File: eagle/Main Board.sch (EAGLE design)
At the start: 3 parts

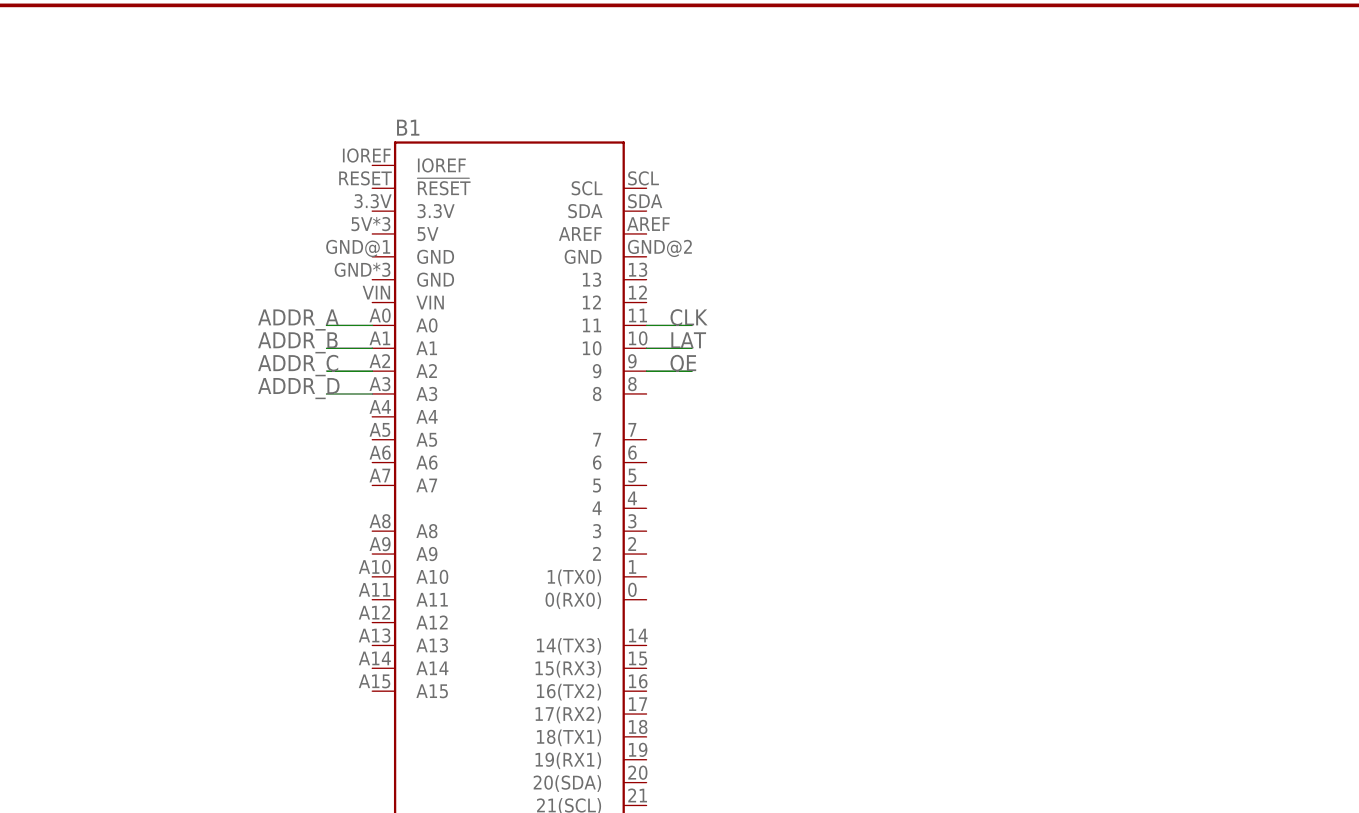
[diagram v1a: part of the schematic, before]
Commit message: Wired rotary encoder to arduino.
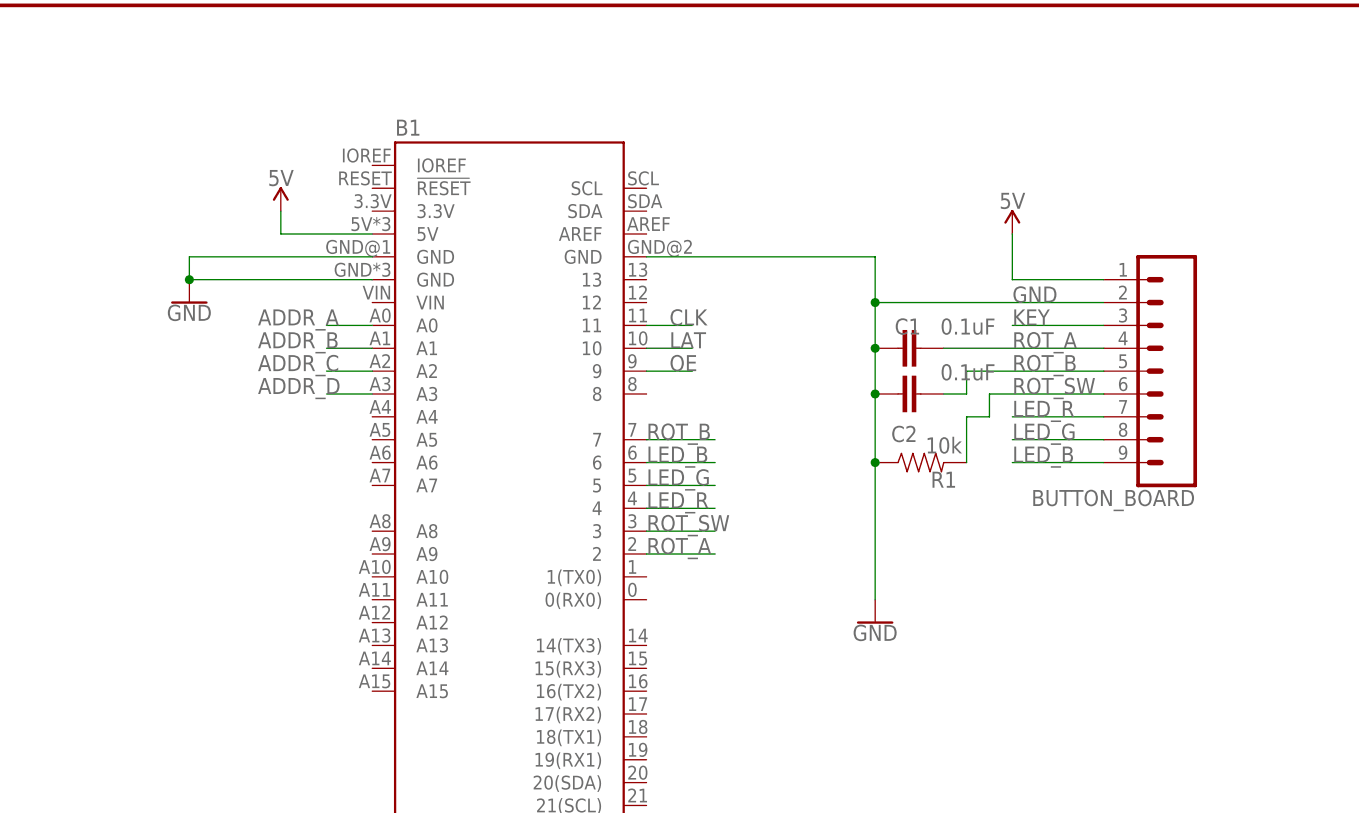
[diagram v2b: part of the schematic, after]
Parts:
- added BUTTON_BOARD: (no value), SparkFun-Connectors:CONN_09
- added C1, C2: 0.1uF, SparkFun-Capacitors:0.1UF-KIT-EZ-50V-20%
- added R1: 10k, SparkFun-Resistors:10KOHM-HORIZ-1/4W-1%
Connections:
- new net 5V: B1.5V, BUTTON_BOARD.1
- new net KEY: BUTTON_BOARD.3
- new net LED_B: B1.6, BUTTON_BOARD.9
- new net LED_G: B1.5, BUTTON_BOARD.8
- new net LED_R: B1.4, BUTTON_BOARD.7
- new net ROT_A: B1.2, BUTTON_BOARD.4, C1.2
- new net ROT_B: B1.7, BUTTON_BOARD.5, C2.2
- new net ROT_SW: B1.3, BUTTON_BOARD.6, R1.2
- net GND: now also B1.GND, B1.GND@2, B1.GND@3, BUTTON_BOARD.2, C1.1, C2.1, R1.1
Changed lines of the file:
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@@
 <part name="J1" library="SparkFun-Connectors" deviceset="CONN_08X2" device="_SHROUD"/>
 <part name="GND1" library="SparkFun-PowerSymbols" deviceset="GND" device=""/>
+<part name="BUTTON_BOARD" library="SparkFun-Connectors" deviceset="CONN_09" device=""/>
+<part name="GND2" library="SparkFun-PowerSymbols" deviceset="GND" device=""/>
+<part name="GND3" library="SparkFun-PowerSymbols" deviceset="GND" device=""/>
+<part name="R1" library="SparkFun-Resistors" deviceset="10KOHM" device="-HORIZ-1/4W-1%" value="10k"/>
+<part name="SUPPLY1" library="SparkFun-PowerSymbols" deviceset="5V" device=""/>
+<part name="SUPPLY2" library="SparkFun-PowerSymbols" deviceset="5V" device=""/>
+<part name="C1" library="SparkFun-Capacitors" deviceset="0.1UF" device="-KIT-EZ-50V-20%" value="0.1uF"/>
+<part name="C2" library="SparkFun-Capacitors" deviceset="0.1UF" device="-KIT-EZ-50V-20%" value="0.1uF"/>
 </parts>
 <sheets>
@@
 <attribute name="VALUE" x="45.72" y="149.606" size="1.778" layer="96" font="vector" align="top-center"/>
 </instance>
+<instance part="BUTTON_BOARD" gate="J1" x="198.12" y="144.78" smashed="yes" rot="R180">
+<attribute name="VALUE" x="198.12" y="159.766" size="1.778" layer="96" font="vector" rot="R180"/>
+<attribute name="NAME" x="198.12" y="131.572" size="1.778" layer="95" font="vector" rot="R180"/>
+</instance>
+<instance part="GND2" gate="1" x="86.36" y="152.4" smashed="yes">
+<attribute name="VALUE" x="86.36" y="152.146" size="1.778" layer="96" font="vector" align="top-center"/>
+</instance>
+<instance part="GND3" gate="1" x="162.56" y="116.84" smashed="yes">
+<attribute name="VALUE" x="162.56" y="116.586" size="1.778" layer="96" font="vector" align="top-center"/>
+</instance>
+<instance part="R1" gate="G$1" x="167.64" y="134.62" smashed="yes">
+<attribute name="NAME" x="170.18" y="133.604" size="1.778" layer="95" font="vector" rot="R180" align="bottom-center"/>
+<attribute name="VALUE" x="170.18" y="135.636" size="1.778" layer="96" font="vector" rot="R180" align="top-center"/>
+</instance>
+<instance part="SUPPLY1" gate="G$1" x="177.8" y="160.02" smashed="yes">
+<attribute name="VALUE" x="177.8" y="162.814" size="1.778" layer="96" font="vector" align="bottom-center"/>
+</instance>
+<instance part="SUPPLY2" gate="G$1" x="96.52" y="162.56" smashed="yes">
+<attribute name="VALUE" x="96.52" y="165.354" size="1.778" layer="96" font="vector" align="bottom-center"/>
+</instance>
+<instance part="C1" gate="G$1" x="167.64" y="147.32" smashed="yes" rot="R90">
+<attribute name="NAME" x="164.719" y="148.844" size="1.778" layer="95" font="vector"/>
+<attribute name="VALUE" x="169.799" y="148.844" size="1.778" layer="96" font="vector"/>
+</instance>
+<instance part="C2" gate="G$1" x="167.64" y="142.24" smashed="yes" rot="R90">
+<attribute name="NAME" x="167.259" y="138.684" size="1.778" layer="95" font="vector" rot="R180"/>
+<attribute name="VALUE" x="169.799" y="143.764" size="1.778" layer="96" font="vector"/>
+</instance>
 </instances>
 <busses>
@@
 <wire x1="35.56" y1="152.4" x2="45.72" y2="152.4" width="0.1524" layer="91"/>
 </segment>
+<segment>
+<pinref part="B1" gate="B1" pin="GND@2"/>
+<pinref part="GND2" gate="1" pin="GND"/>
+<wire x1="106.68" y1="157.48" x2="86.36" y2="157.48" width="0.1524" layer="91"/>
+<wire x1="86.36" y1="157.48" x2="86.36" y2="154.94" width="0.1524" layer="91"/>
+<pinref part="B1" gate="B1" pin="GND"/>
+<wire x1="106.68" y1="154.94" x2="86.36" y2="154.94" width="0.1524" layer="91"/>
+<junction x="86.36" y="154.94"/>
+</segment>
+<segment>
+<pinref part="C1" gate="G$1" pin="1"/>
+<pinref part="C2" gate="G$1" pin="1"/>
+<wire x1="162.56" y1="147.32" x2="162.56" y2="142.24" width="0.1524" layer="91"/>
+<pinref part="BUTTON_BOARD" gate="J1" pin="2"/>
+<wire x1="187.96" y1="152.4" x2="162.56" y2="152.4" width="0.1524" layer="91"/>
+<wire x1="162.56" y1="152.4" x2="162.56" y2="147.32" width="0.1524" layer="91"/>
+<junction x="162.56" y="147.32"/>
+<pinref part="B1" gate="B1" pin="GND@3"/>
+<wire x1="137.16" y1="157.48" x2="162.56" y2="157.48" width="0.1524" layer="91"/>
+<wire x1="162.56" y1="157.48" x2="162.56" y2="152.4" width="0.1524" layer="91"/>
+<junction x="162.56" y="152.4"/>
+<pinref part="R1" gate="G$1" pin="1"/>
+<wire x1="162.56" y1="142.24" x2="162.56" y2="134.62" width="0.1524" layer="91"/>
+<junction x="162.56" y="142.24"/>
+<pinref part="GND3" gate="1" pin="GND"/>
+<wire x1="162.56" y1="134.62" x2="162.56" y2="119.38" width="0.1524" layer="91"/>
+<junction x="162.56" y="134.62"/>
+<label x="177.8" y="152.4" size="1.778" layer="95"/>
+</segment>
+</net>
+<net name="ROT_A" class="0">
+<segment>
+<pinref part="B1" gate="B1" pin="2"/>
+<wire x1="137.16" y1="124.46" x2="144.78" y2="124.46" width="0.1524" layer="91"/>
+<label x="137.16" y="124.46" size="1.778" layer="95"/>
+</segment>
+<segment>
+<pinref part="BUTTON_BOARD" gate="J1" pin="4"/>
+<wire x1="187.96" y1="147.32" x2="170.18" y2="147.32" width="0.1524" layer="91"/>
+<label x="177.8" y="147.32" size="1.778" layer="95"/>
+<pinref part="C1" gate="G$1" pin="2"/>
+</segment>
+</net>
+<net name="5V" class="0">
+<segment>
+<pinref part="B1" gate="B1" pin="5V"/>
+<wire x1="106.68" y1="160.02" x2="96.52" y2="160.02" width="0.1524" layer="91"/>
+<wire x1="96.52" y1="160.02" x2="96.52" y2="162.56" width="0.1524" layer="91"/>
+<pinref part="SUPPLY2" gate="G$1" pin="5V"/>
+</segment>
+<segment>
+<pinref part="BUTTON_BOARD" gate="J1" pin="1"/>
+<pinref part="SUPPLY1" gate="G$1" pin="5V"/>
+<wire x1="187.96" y1="154.94" x2="177.8" y2="154.94" width="0.1524" layer="91"/>
+<wire x1="177.8" y1="154.94" x2="177.8" y2="160.02" width="0.1524" layer="91"/>
+</segment>
+</net>
+<net name="ROT_SW" class="0">
+<segment>
+<pinref part="B1" gate="B1" pin="3"/>
+<wire x1="137.16" y1="127" x2="144.78" y2="127" width="0.1524" layer="91"/>
+<label x="137.16" y="127" size="1.778" layer="95"/>
+</segment>
+<segment>
+<pinref part="BUTTON_BOARD" gate="J1" pin="6"/>
+<wire x1="187.96" y1="142.24" x2="175.26" y2="142.24" width="0.1524" layer="91"/>
+<label x="177.8" y="142.24" size="1.778" layer="95"/>
+<wire x1="175.26" y1="142.24" x2="175.26" y2="139.7" width="0.1524" layer="91"/>
+<pinref part="R1" gate="G$1" pin="2"/>
+<wire x1="175.26" y1="139.7" x2="172.72" y2="139.7" width="0.1524" layer="91"/>
+<wire x1="172.72" y1="139.7" x2="172.72" y2="134.62" width="0.1524" layer="91"/>
+</segment>
+</net>
+<net name="LED_R" class="0">
+<segment>
+<pinref part="B1" gate="B1" pin="4"/>
+<wire x1="137.16" y1="129.54" x2="144.78" y2="129.54" width="0.1524" layer="91"/>
+<label x="137.16" y="129.54" size="1.778" layer="95"/>
+</segment>
+<segment>
+<pinref part="BUTTON_BOARD" gate="J1" pin="7"/>
+<wire x1="187.96" y1="139.7" x2="177.8" y2="139.7" width="0.1524" layer="91"/>
+<label x="177.8" y="139.7" size="1.778" layer="95"/>
+</segment>
+</net>
+<net name="LED_G" class="0">
+<segment>
+<pinref part="B1" gate="B1" pin="5"/>
+<wire x1="137.16" y1="132.08" x2="144.78" y2="132.08" width="0.1524" layer="91"/>
+<label x="137.16" y="132.08" size="1.778" layer="95"/>
+</segment>
+<segment>
+<pinref part="BUTTON_BOARD" gate="J1" pin="8"/>
+<wire x1="187.96" y1="137.16" x2="177.8" y2="137.16" width="0.1524" layer="91"/>
+<label x="177.8" y="137.16" size="1.778" layer="95"/>
+</segment>
+</net>
+<net name="LED_B" class="0">
+<segment>
+<pinref part="B1" gate="B1" pin="6"/>
+<wire x1="137.16" y1="134.62" x2="144.78" y2="134.62" width="0.1524" layer="91"/>
+<label x="137.16" y="134.62" size="1.778" layer="95"/>
+</segment>
+<segment>
+<pinref part="BUTTON_BOARD" gate="J1" pin="9"/>
+<wire x1="187.96" y1="134.62" x2="177.8" y2="134.62" width="0.1524" layer="91"/>
+<label x="177.8" y="134.62" size="1.778" layer="95"/>
+</segment>
+</net>
+<net name="ROT_B" class="0">
+<segment>
+<pinref part="B1" gate="B1" pin="7"/>
+<wire x1="137.16" y1="137.16" x2="144.78" y2="137.16" width="0.1524" layer="91"/>
+<label x="137.16" y="137.16" size="1.778" layer="95"/>
+</segment>
+<segment>
+<pinref part="BUTTON_BOARD" gate="J1" pin="5"/>
+<wire x1="187.96" y1="144.78" x2="172.72" y2="144.78" width="0.1524" layer="91"/>
+<label x="177.8" y="144.78" size="1.778" layer="95"/>
+<wire x1="172.72" y1="144.78" x2="172.72" y2="142.24" width="0.1524" layer="91"/>
+<pinref part="C2" gate="G$1" pin="2"/>
+<wire x1="172.72" y1="142.24" x2="170.18" y2="142.24" width="0.1524" layer="91"/>
+</segment>
+</net>
+<net name="KEY" class="0">
+<segment>
+<pinref part="BUTTON_BOARD" gate="J1" pin="3"/>
+<wire x1="187.96" y1="149.86" x2="177.8" y2="149.86" width="0.1524" layer="91"/>
+<label x="177.8" y="149.86" size="1.778" layer="95"/>
+</segment>
 </net>
 </nets>
@@
 </schematic>
 </drawing>
+<compatibility>
+<note version="8.3" severity="warning">
+Since Version 8.3, EAGLE supports URNs for individual library
+assets (packages, symbols, and devices). The URNs of those assets
+will not be understood (or retained) with this version.
+</note>
+</compatibility>
 </eagle>
